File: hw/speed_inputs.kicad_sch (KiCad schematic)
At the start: 21 parts, among them U701 COMPARATOR_GENERIC

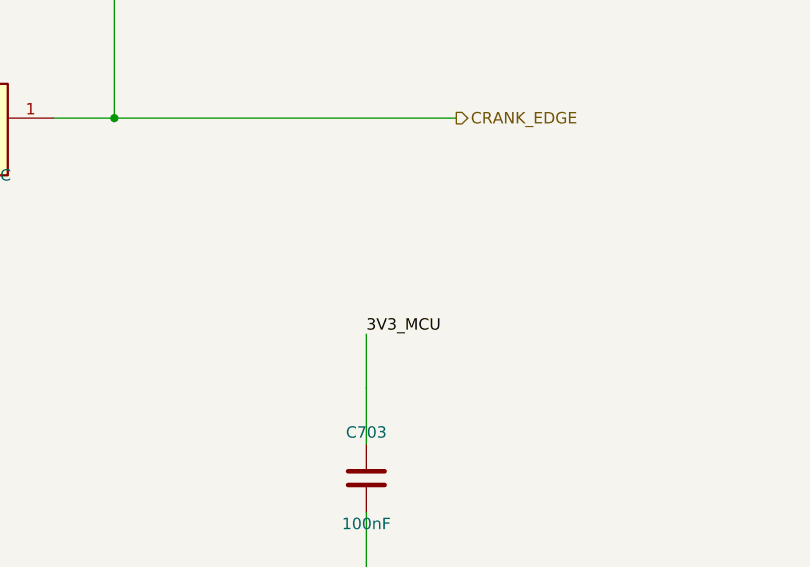
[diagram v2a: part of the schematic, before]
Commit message: Check the project netlist, and fix the three things it caught
hw/check_netlist.py grew the two checks that found them, so neither can
come back quietly. It is the counterpart to sim/run_sim.py: that one
guards the component values, this one guards the connectivity.

5V_MAIN WAS FOUR NETS. The buck's 5 V output is a board rail -- both CAN
transceivers' VCC, the five difference amplifiers and the discrete
inputs' pull-ups run off it -- and it was a LOCAL label on every one of
those sheets. A local label stops at its sheet's edge, so three of the
four copies had no regulator on them. Each sheet's own netlist was
correct, which is exactly why ten clean per-sheet netlists never found
it. rails now exports it as a hierarchical label.

3V3_MCU WAS THREE. Same mechanism on can (both transceivers' VIO) and
speed_inputs, where the comparator's supply, both upper clamp diodes and
the bias divider sat on a five-pin net with no rail attached.

New check: any sheet-local net whose name shadows a project-wide net
name fails. That is the exact shape of both defects.

FIVE SUPPLY PINS HAD NO DECOUPLING CAPACITOR. The difference amplifiers
on sensors_analog were the only undecoupled supply pins on the board. No
simulation block was ever going to say so -- sensor_differential.cir
models an ideal amplifier with no supply pin at all. 100 nF each, at the
pin.

New check: walk every power_in pin in the project netlist and ask
whether a capacitor sits on the same net. 22 supply pins, all covered.
One documented exemption, the LM5164's BST pin, whose bootstrap
capacitor IS the net.

Gate now: 201 components with unique references, 108 named nets carrying
two or more pins, 18 reaching one and each a recorded open item, GND 139
pins, 3V3_MCU 36, 5V_MAIN 28, VBAT_PROT 12.

Schematic set re-plotted: docs/pdf/ECU-Schematics.pdf, 11 pages.
Suite still 24/24.

Co-Authored-By: Claude Opus 5 <noreply@anthropic.com>
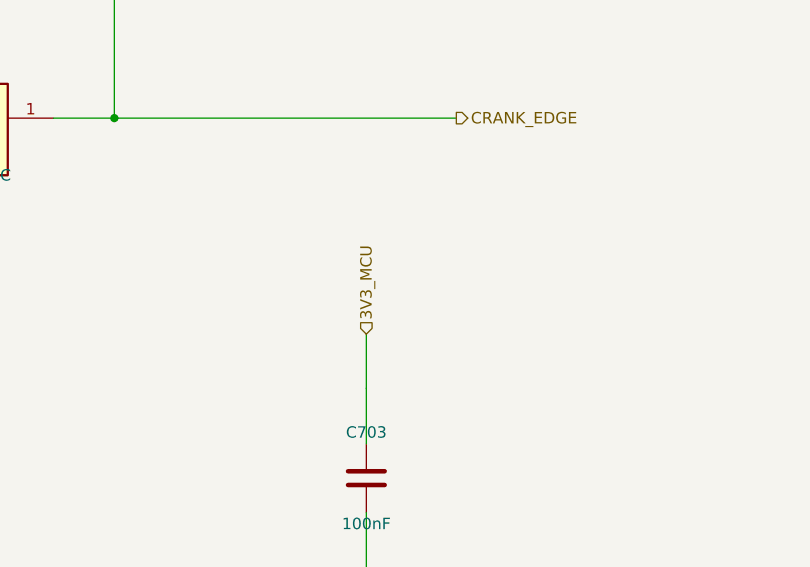
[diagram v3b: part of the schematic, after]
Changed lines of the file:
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@@
     (stroke (width 0) (type default))
   )
-  (label "3V3_MCU" (at 300.0 94.0 0)
-    (effects (font (size 1.27 1.27)) (justify left bottom))
+  (hierarchical_label "3V3_MCU" (shape input) (at 300.0 94.0 90)
+    (effects (font (size 1.27 1.27)) (justify left))
   )
   (symbol (lib_id "Device:C") (at 300.0 110.0 0) (unit 1)

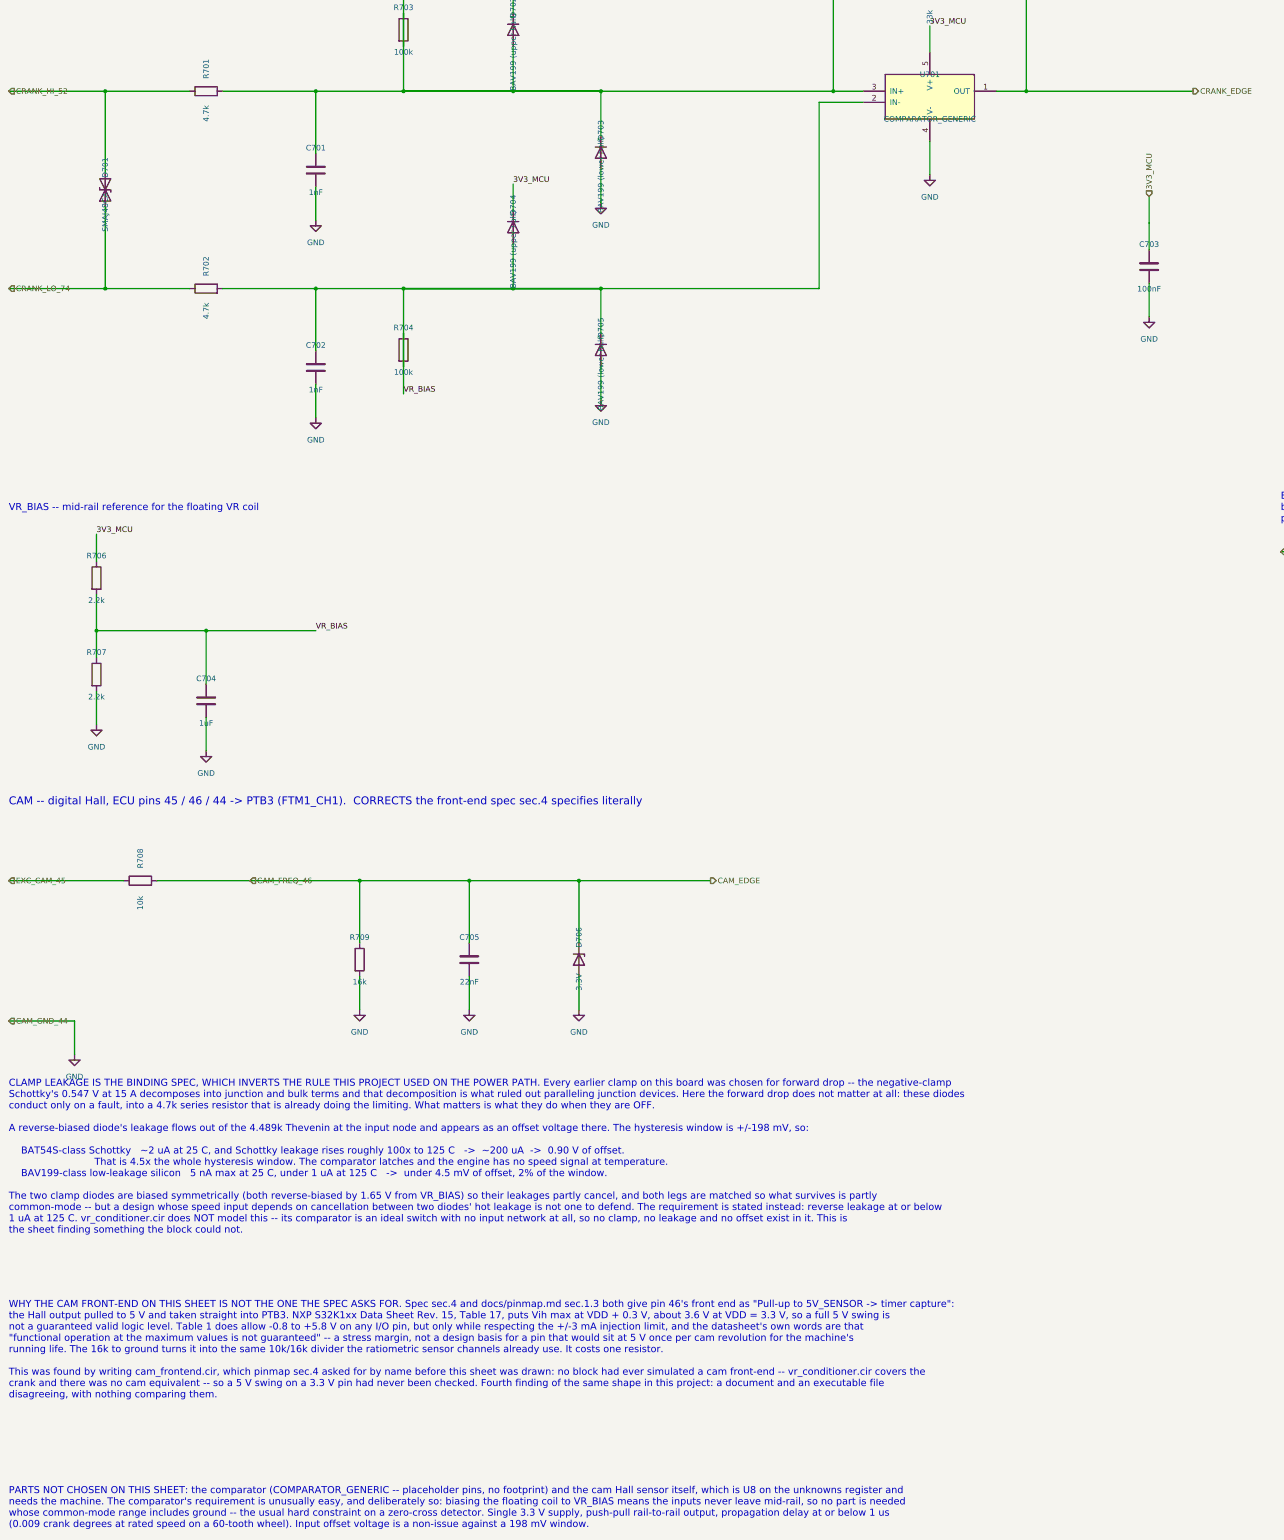
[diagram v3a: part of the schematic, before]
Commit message: Replace the crank comparator placeholder with TLV3201-Q1
The part already chosen for the negative clamp meets every line of
VR-COMP, so one part number now serves both: single 3.3 V (2.7-5.5 V),
push-pull, input range (VEE)-0.2 V to (VCC)+0.2 V around the 1.65 V
VR_BIAS, 50 ns max against a 1 us requirement, and a 5 mV max offset
against the +/-198 mV hysteresis window.

Push-pull was the requirement that mattered: the output swing IS the
hysteresis window (3.3 V x 4489 / 37489), so an open-drain part would
have made the window depend on a pull-up and on VOL.

Same pin positions as COMPARATOR_GENERIC; IN- and GND carry different
numbers (4 and 2, not 2 and 4) and the generator reads pins by number,
so both were swapped. Netlist confirms IN+ on the HI leg, IN- on the LO
leg.

Co-Authored-By: Claude Opus 5 <noreply@anthropic.com>
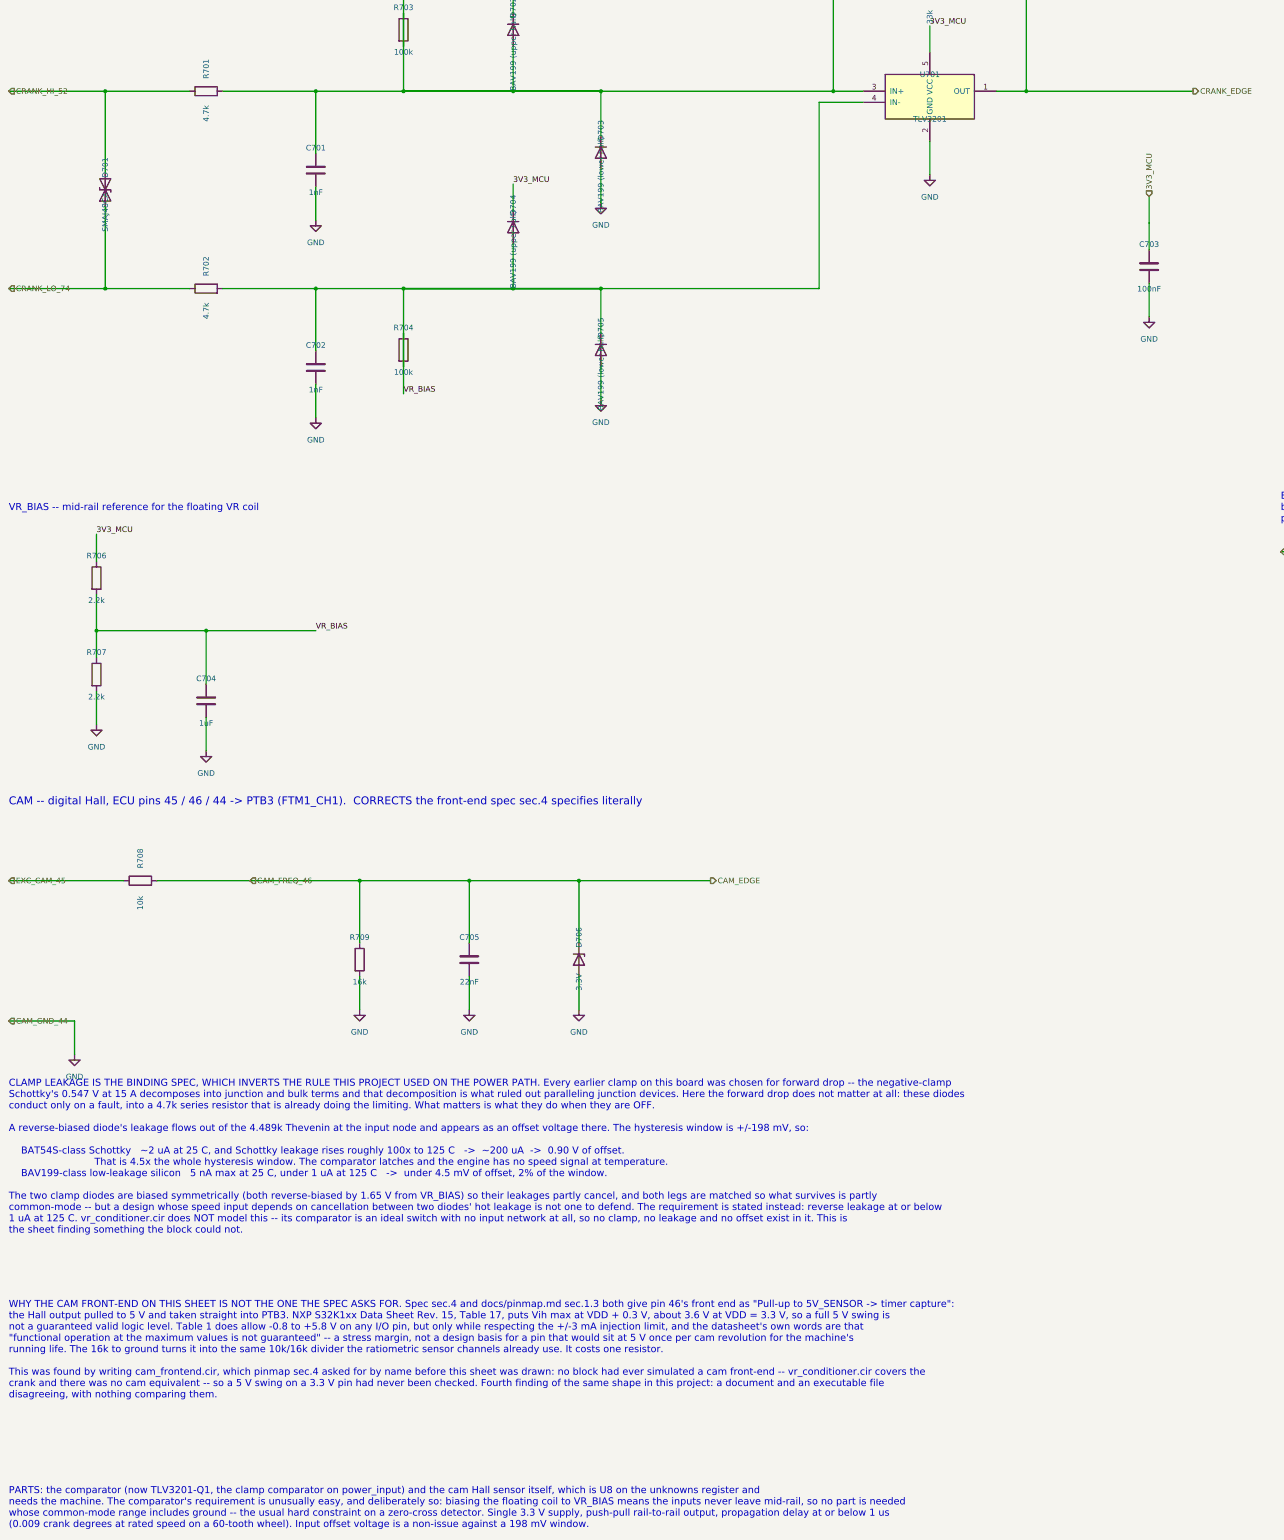
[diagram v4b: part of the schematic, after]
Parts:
- removed U701: COMPARATOR_GENERIC, symbol ecu25kva:COMPARATOR_GENERIC
- added U701: TLV3201, Package_TO_SOT_SMD:SOT-353_SC-70-5, symbol ecu25kva:TLV3201
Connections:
- net 3V3_MCU: now also U701.5 (VCC)
- net CRANK_EDGE: now also U701.1 (OUT)
- net GND: now also U701.2 (GND)
- net VR_BIAS: now also U701.3 (IN+), U701.4 (IN-)
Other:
- note added: "PARTS: the comparator (now TLV3201-Q1, the clamp comparator on power_input) and the cam Hall sensor itself, which is U8 on the unknowns register and needs the machine. The comparator's requirement is unusually easy, and deliberately so: biasing the floating coil to VR_BIAS means the inputs never leave mid-rail, so no part is needed whose common-mode range includes ground -- the usual hard constra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"
- note removed: "PARTS NOT CHOSEN ON THIS SHEET: the comparator (COMPARATOR_GENERIC -- placeholder pins, no footprint) and the cam Hall sensor itself, which is U8 on the unknowns register and needs the machine. The comparator's requirement is unusually easy, and deliberately so: biasing the floating coil to VR_BIAS means the inputs never leave mid-rail, so no part is needed whose common-mode range includes ground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"
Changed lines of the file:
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@@
     (effects (font (size 1.8 1.8)) (justify left))
   )
-  (symbol (lib_id "ecu25kva:COMPARATOR_GENERIC") (at 250.0 71.27 0) (unit 1)
+  (symbol (lib_id "ecu25kva:TLV3201") (at 250.0 71.27 0) (unit 1)
     (in_bom yes) (on_board yes) (fields_autoplaced)
     (property "Reference" "U701" (id 0) (at 250.0 66.19 0)
       (effects (font (size 1.27 1.27)))
     )
-    (property "Value" "COMPARATOR_GENERIC" (id 1) (at 250.0 76.35 0)
-      (effects (font (size 1.27 1.27)))
-    )
-    (property "Footprint" "" (id 2) (at 250.0 71.27 0)
+    (property "Value" "TLV3201" (id 1) (at 250.0 76.35 0)
+      (effects (font (size 1.27 1.27)))
+    )
+    (property "Footprint" "Package_TO_SOT_SMD:SOT-353_SC-70-5" (id 2) (at 250.0 71.27 0)
       (effects (font (size 1.27 1.27)) hide)
     )
@@
       (effects (font (size 1.27 1.27)) hide)
     )
-    (property "Source" "vr_conditioner.cir -- ZCSW" (id 4) (at 250.0 71.27 0)
-      (effects (font (size 1.27 1.27)) hide)
-    )
-    (property "Requirement" "single 3.3 V supply, PUSH-PULL rail-to-rail output, mid-rail input common-mode, prop delay <=1 us" (id 5) (at 250.0 71.27 0)
-      (effects (font (size 1.27 1.27)) hide)
-    )
-    (property "Note" "Part NOT chosen -- placeholder pin numbers, no footprint. The output swing sets the hysteresis window, so an open-drain part would make the window depend on its pull-up and its VOL." (id 6) (at 250.0 71.27 0)
+    (property "Source" "TI SBOS856A; vr_conditioner.cir -- ZCSW" (id 4) (at 250.0 71.27 0)
+      (effects (font (size 1.27 1.27)) hide)
+    )
+    (property "Requirement" "VR-COMP: single 3.3 V, push-pull, mid-rail input, <=1 us -- all met" (id 5) (at 250.0 71.27 0)
+      (effects (font (size 1.27 1.27)) hide)
+    )
+    (property "Note" "The output swing sets the hysteresis window (3.3 V x 4489 / 37489 = +/-198 mV), which is why a push-pull part was required. Its own 1.2 mV internal hysteresis adds nothing that matters against that." (id 6) (at 250.0 71.27 0)
       (effects (font (size 1.27 1.27)) hide)
     )
@@
     (effects (font (size 1.6 1.6)) (justify left))
   )
-  (text "PARTS NOT CHOSEN ON THIS SHEET: the comparator (COMPARATOR_GENERIC -- placeholder pins, no footprint) and the cam Hall sensor itself, which is U8 on the unknowns register and\nneeds the machine. The comparator's requirement is unusually easy, and deliberately so: biasing the floating coil to VR_BIAS means the inputs never leave mid-rail, so no part is needed\nwhose common-mode range includes ground -- the usual hard constraint on a zero-cross detector. Single 3.3 V supply, push-pull rail-to-rail output, propagation delay at or below 1 us\n(0.009 crank degrees at rated speed on a 60-tooth wheel). Input offset voltage is a non-issue against a 198 mV window." (at 40.0 393.0 0)
+  (text "PARTS: the comparator (now TLV3201-Q1, the clamp comparator on power_input) and the cam Hall sensor itself, which is U8 on the unknowns register and\nneeds the machine. The comparator's requirement is unusually easy, and deliberately so: biasing the floating coil to VR_BIAS means the inputs never leave mid-rail, so no part is needed\nwhose common-mode range includes ground -- the usual hard constraint on a zero-cross detector. Single 3.3 V supply, push-pull rail-to-rail output, propagation delay at or below 1 us\n(0.009 crank degrees at rated speed on a 60-tooth wheel). Input offset voltage is a non-issue against a 198 mV window." (at 40.0 393.0 0)
     (effects (font (size 1.6 1.6)) (justify left))
   )
